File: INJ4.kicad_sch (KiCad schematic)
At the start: 8 parts, among them Q1 VND14NV04-E, Q2 VND14NV04-E, Q3 VND14NV04-E, Q4 VND14NV04-E

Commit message: Vendor DPAK/R0603 footprints for Update PCB without submodule gaps
Frame inj/LS sheets now use microcore-fp (in-repo footprints/) so KiCad
finds DPAK and R0603 even when hellen-one-common is missing from a zip
checkout. Keep hellen-one-common for Mini-B and other shared parts.
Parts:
- Q1, Q2, Q3, Q4: footprint hellen-one-common:DPAK -> microcore-fp:DPAK
- R1, R2, R3, R4: footprint hellen-one-common:R0603 -> microcore-fp:R0603
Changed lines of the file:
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@@
 			)
 		)
-		(property "Footprint" "hellen-one-common:DPAK"
+		(property "Footprint" "microcore-fp:DPAK"
 			(at 101.6 25.4 0)
 			(effects
@@
 			)
 		)
-		(property "Footprint" "hellen-one-common:R0603"
+		(property "Footprint" "microcore-fp:R0603"
 			(at 139.7 25.4 0)
 			(effects
@@
 			)
 		)
-		(property "Footprint" "hellen-one-common:DPAK"
+		(property "Footprint" "microcore-fp:DPAK"
 			(at 101.6 55.879999999999995 0)
 			(effects
@@
 			)
 		)
-		(property "Footprint" "hellen-one-common:R0603"
+		(property "Footprint" "microcore-fp:R0603"
 			(at 139.7 55.879999999999995 0)
 			(effects
@@
 			)
 		)
-		(property "Footprint" "hellen-one-common:DPAK"
+		(property "Footprint" "microcore-fp:DPAK"
 			(at 101.6 86.36 0)
 			(effects
@@
 			)
 		)
-		(property "Footprint" "hellen-one-common:R0603"
+		(property "Footprint" "microcore-fp:R0603"
 			(at 139.7 86.36 0)
 			(effects
@@
 			)
 		)
-		(property "Footprint" "hellen-one-common:DPAK"
+		(property "Footprint" "microcore-fp:DPAK"
 			(at 101.6 116.84 0)
 			(effects
@@
 			)
 		)
-		(property "Footprint" "hellen-one-common:R0603"
+		(property "Footprint" "microcore-fp:R0603"
 			(at 139.7 116.84 0)
 			(effects

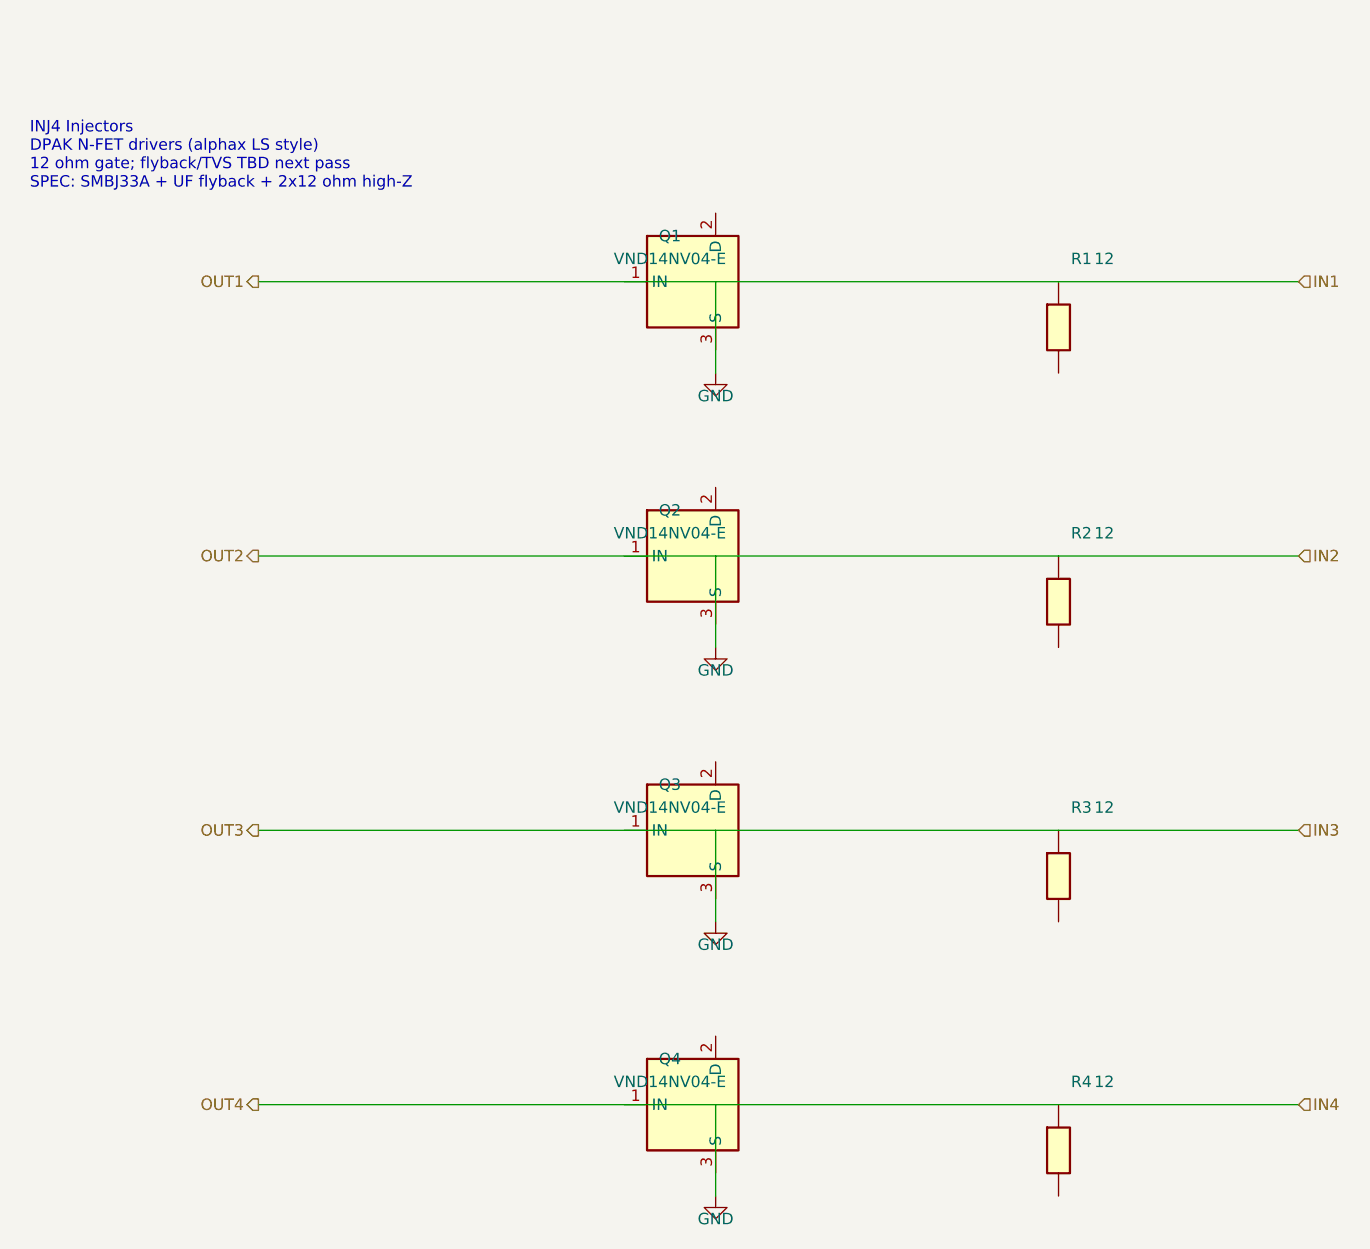
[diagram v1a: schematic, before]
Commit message: Fix top schematic wiring so labels connect to Hellen module pins
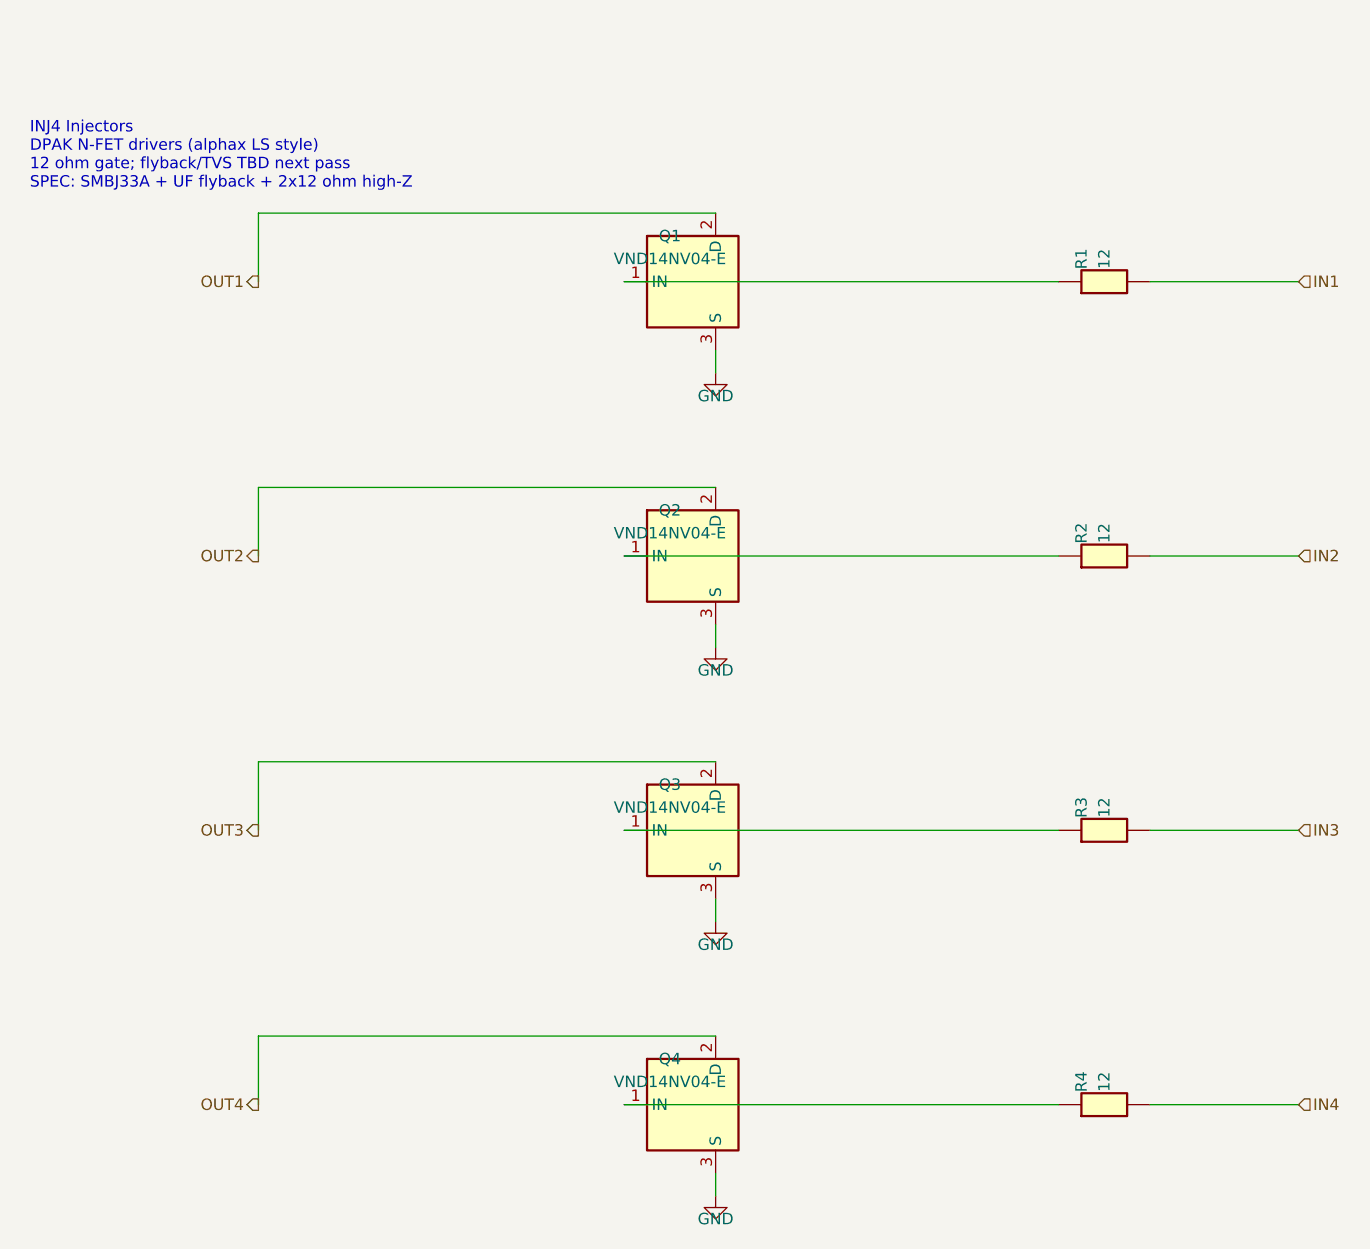
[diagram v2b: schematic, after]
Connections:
- net GND: now also Q1.3 (S), Q2.3 (S), Q3.3 (S), Q4.3 (S); no longer R1.1, R2.1, R3.1, R4.1
- net at Q4.1 (IN): now also R4.1
- net OUT4: now reaches Q4.2 (D)
- net IN1: now reaches R1.2
- net IN4: now reaches R4.2
- net IN3: now reaches R3.2
- net at Q3.1 (IN): now also R3.1
- net OUT3: now reaches Q3.2 (D)
- net at Q1.1 (IN): now also R1.1
- net OUT1: now reaches Q1.2 (D)
- net IN2: now reaches R2.2
- net at Q2.1 (IN): now also R2.1
- net OUT2: now reaches Q2.2 (D)
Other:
- moved on the sheet: R1, R2, R3, R4
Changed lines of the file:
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@@
 	(symbol
 		(lib_id "hellen-one-common:Res")
-		(at 139.7 25.4 270)
+		(at 139.7 25.4 0)
 		(unit 1)
 		(exclude_from_sim no)
@@
 	(symbol
 		(lib_id "hellen-one-common:Res")
-		(at 139.7 55.879999999999995 270)
+		(at 139.7 55.879999999999995 0)
 		(unit 1)
 		(exclude_from_sim no)
@@
 	(symbol
 		(lib_id "hellen-one-common:Res")
-		(at 139.7 86.36 270)
+		(at 139.7 86.36 0)
 		(unit 1)
 		(exclude_from_sim no)
@@
 	(symbol
 		(lib_id "hellen-one-common:Res")
-		(at 139.7 116.84 270)
+		(at 139.7 116.84 0)
 		(unit 1)
 		(exclude_from_sim no)
@@
 		)
 	)
-	(wire
-		(pts
-			(xy 50.8 25.4) (xy 101.6 25.4)
-		)
-		(stroke
-			(width 0)
-			(type default)
-		)
-	)
-	(wire
-		(pts
-			(xy 101.6 25.4) (xy 139.7 25.4)
-		)
-		(stroke
-			(width 0)
-			(type default)
-		)
-	)
-	(wire
-		(pts
-			(xy 139.7 25.4) (xy 166.37 25.4)
-		)
-		(stroke
-			(width 0)
-			(type default)
-		)
-	)
-	(wire
-		(pts
-			(xy 101.6 25.4) (xy 101.6 35.56)
-		)
-		(stroke
-			(width 0)
-			(type default)
-		)
-	)
-	(wire
-		(pts
-			(xy 50.8 55.879999999999995) (xy 101.6 55.879999999999995)
-		)
-		(stroke
-			(width 0)
-			(type default)
-		)
-	)
-	(wire
-		(pts
-			(xy 101.6 55.879999999999995) (xy 139.7 55.879999999999995)
-		)
-		(stroke
-			(width 0)
-			(type default)
-		)
-	)
-	(wire
-		(pts
-			(xy 139.7 55.879999999999995) (xy 166.37 55.879999999999995)
-		)
-		(stroke
-			(width 0)
-			(type default)
-		)
-	)
-	(wire
-		(pts
-			(xy 101.6 55.879999999999995) (xy 101.6 66.03999999999999)
-		)
-		(stroke
-			(width 0)
-			(type default)
-		)
-	)
-	(wire
-		(pts
-			(xy 50.8 86.36) (xy 101.6 86.36)
-		)
-		(stroke
-			(width 0)
-			(type default)
-		)
-	)
-	(wire
-		(pts
-			(xy 101.6 86.36) (xy 139.7 86.36)
-		)
-		(stroke
-			(width 0)
-			(type default)
-		)
-	)
-	(wire
-		(pts
-			(xy 139.7 86.36) (xy 166.37 86.36)
-		)
-		(stroke
-			(width 0)
-			(type default)
-		)
-	)
-	(wire
-		(pts
-			(xy 101.6 86.36) (xy 101.6 96.52)
-		)
-		(stroke
-			(width 0)
-			(type default)
-		)
-	)
-	(wire
-		(pts
-			(xy 50.8 116.84) (xy 101.6 116.84)
-		)
-		(stroke
-			(width 0)
-			(type default)
-		)
-	)
-	(wire
-		(pts
-			(xy 101.6 116.84) (xy 139.7 116.84)
-		)
-		(stroke
-			(width 0)
-			(type default)
-		)
-	)
-	(wire
-		(pts
-			(xy 139.7 116.84) (xy 166.37 116.84)
-		)
-		(stroke
-			(width 0)
-			(type default)
-		)
-	)
-	(wire
-		(pts
-			(xy 101.6 116.84) (xy 101.6 127.0)
-		)
-		(stroke
-			(width 0)
-			(type default)
-		)
-	)
 	(text "INJ4 Injectors\nDPAK N-FET drivers (alphax LS style)\n12 ohm gate; flyback/TVS TBD next pass\nSPEC: SMBJ33A + UF flyback + 2x12 ohm high-Z"
 		(at 25.4 15.24 0)
@@
 		)
 	)
+	(wire
+		(pts
+			(xy 50.8 25.4) (xy 50.8 17.78)
+		)
+		(stroke
+			(width 0)
+			(type default)
+		)
+	)
+	(wire
+		(pts
+			(xy 50.8 17.78) (xy 101.6 17.78)
+		)
+		(stroke
+			(width 0)
+			(type default)
+		)
+	)
+	(wire
+		(pts
+			(xy 101.6 33.02) (xy 101.6 35.56)
+		)
+		(stroke
+			(width 0)
+			(type default)
+		)
+	)
+	(wire
+		(pts
+			(xy 166.37 25.4) (xy 149.86 25.4)
+		)
+		(stroke
+			(width 0)
+			(type default)
+		)
+	)
+	(wire
+		(pts
+			(xy 139.7 25.4) (xy 91.44 25.4)
+		)
+		(stroke
+			(width 0)
+			(type default)
+		)
+	)
+	(wire
+		(pts
+			(xy 50.8 55.88) (xy 50.8 48.26)
+		)
+		(stroke
+			(width 0)
+			(type default)
+		)
+	)
+	(wire
+		(pts
+			(xy 50.8 48.26) (xy 101.6 48.26)
+		)
+		(stroke
+			(width 0)
+			(type default)
+		)
+	)
+	(wire
+		(pts
+			(xy 101.6 63.5) (xy 101.6 66.04)
+		)
+		(stroke
+			(width 0)
+			(type default)
+		)
+	)
+	(wire
+		(pts
+			(xy 166.37 55.88) (xy 149.86 55.88)
+		)
+		(stroke
+			(width 0)
+			(type default)
+		)
+	)
+	(wire
+		(pts
+			(xy 139.7 55.88) (xy 91.44 55.88)
+		)
+		(stroke
+			(width 0)
+			(type default)
+		)
+	)
+	(wire
+		(pts
+			(xy 50.8 86.36) (xy 50.8 78.74)
+		)
+		(stroke
+			(width 0)
+			(type default)
+		)
+	)
+	(wire
+		(pts
+			(xy 50.8 78.74) (xy 101.6 78.74)
+		)
+		(stroke
+			(width 0)
+			(type default)
+		)
+	)
+	(wire
+		(pts
+			(xy 101.6 93.98) (xy 101.6 96.52)
+		)
+		(stroke
+			(width 0)
+			(type default)
+		)
+	)
+	(wire
+		(pts
+			(xy 166.37 86.36) (xy 149.86 86.36)
+		)
+		(stroke
+			(width 0)
+			(type default)
+		)
+	)
+	(wire
+		(pts
+			(xy 139.7 86.36) (xy 91.44 86.36)
+		)
+		(stroke
+			(width 0)
+			(type default)
+		)
+	)
+	(wire
+		(pts
+			(xy 50.8 116.84) (xy 50.8 109.22)
+		)
+		(stroke
+			(width 0)
+			(type default)
+		)
+	)
+	(wire
+		(pts
+			(xy 50.8 109.22) (xy 101.6 109.22)
+		)
+		(stroke
+			(width 0)
+			(type default)
+		)
+	)
+	(wire
+		(pts
+			(xy 101.6 124.46) (xy 101.6 127)
+		)
+		(stroke
+			(width 0)
+			(type default)
+		)
+	)
+	(wire
+		(pts
+			(xy 166.37 116.84) (xy 149.86 116.84)
+		)
+		(stroke
+			(width 0)
+			(type default)
+		)
+	)
+	(wire
+		(pts
+			(xy 139.7 116.84) (xy 91.44 116.84)
+		)
+		(stroke
+			(width 0)
+			(type default)
+		)
+	)

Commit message: Rev j: injector SMAJ33A TVS, US1M flyback, and 2nd 12Ω per INJ channel
SPEC power-stage protection on INJ4 sch+PCB: R8–R11 ballast, D1–D4 US1M,
D5–D8 SMAJ33A (DO-214AC equivalent of SMBJ33A). FET cluster left in place;
new parts in alley + pocket C. BOARD_REVISION bumped to j. PCB remains
substantial (zones + aux origin intact).

Co-authored-by: Quintin <quintinbannink42@users.noreply.github.com>
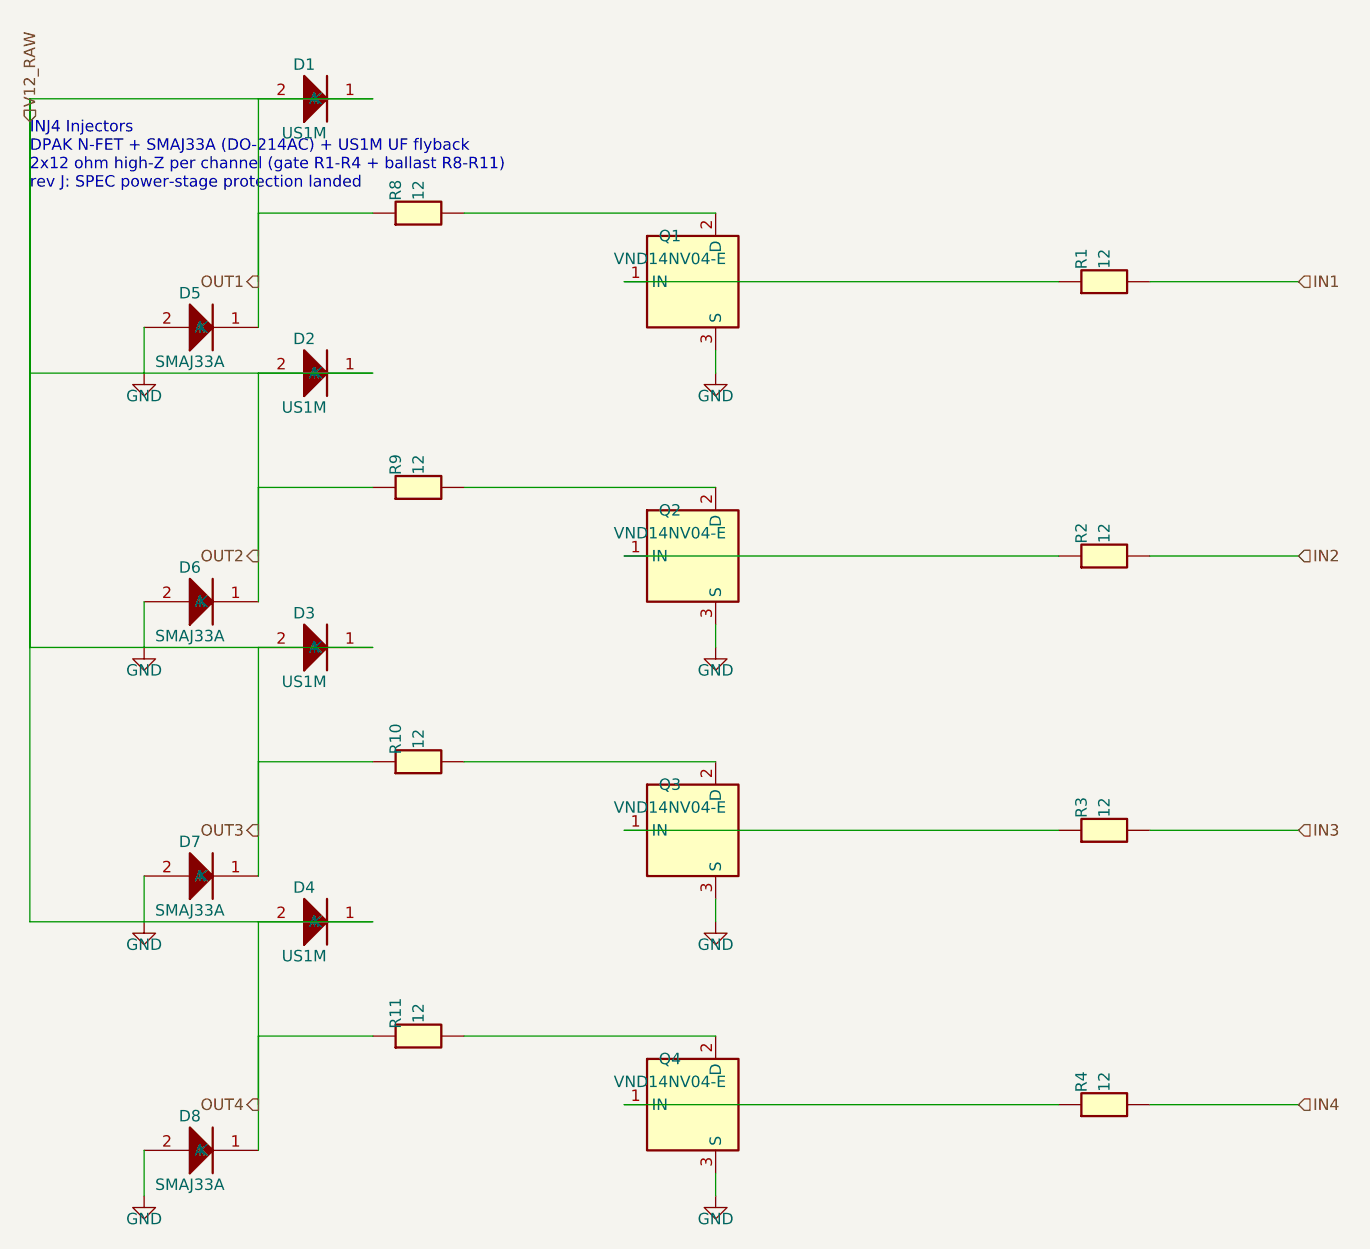
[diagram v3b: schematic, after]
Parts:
- added D1, D2, D3, D4: US1M, microcore-fp:DO214AC, symbol hellen-one-common:1N4148WS
- added D5, D6, D7, D8: SMAJ33A, microcore-fp:DO214AC, symbol hellen-one-common:1N4148WS
- added R10, R11, R8, R9: 12, microcore-fp:R0603, symbol hellen-one-common:Res
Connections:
- net GND: now also D5.2 (A), D6.2 (A), D7.2 (A), D8.2 (A)
- net OUT1: now also D1.2 (A), D5.1 (K), R8.1; no longer Q1.2 (D)
- net OUT2: now also D2.2 (A), D6.1 (K), R9.1; no longer Q2.2 (D)
- net OUT3: now also D3.2 (A), D7.1 (K), R10.1; no longer Q3.2 (D)
- net OUT4: now also D4.2 (A), D8.1 (K), R11.1; no longer Q4.2 (D)
- new net: Q4.2 (D), R11.2
- new net: Q3.2 (D), R10.2
- new net: Q2.2 (D), R9.2
- new net: Q1.2 (D), R8.2
- new net V12_RAW: D1.1 (K), D2.1 (K), D3.1 (K), D4.1 (K)
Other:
- note added: "INJ4 Injectors DPAK N-FET + SMAJ33A (DO-214AC) + US1M UF flyback 2x12 ohm high-Z per channel (gate R1-R4 + ballast R8-R11) rev J: SPEC power-stage protection landed"
- note removed: "INJ4 Injectors DPAK N-FET drivers (alphax LS style) 12 ohm gate; flyback/TVS TBD next pass SPEC: SMBJ33A + UF flyback + 2x12 ohm high-Z"

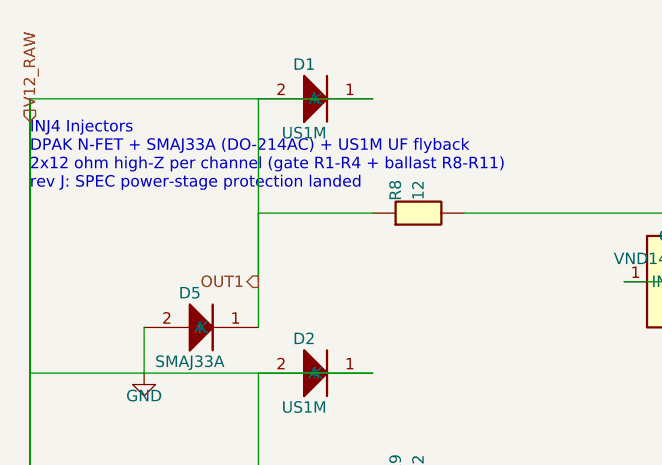
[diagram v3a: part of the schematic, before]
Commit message: Rev k: move injector diodes to B.Cu near J1; drop frame buttons
Flip D1-D4 (US1M) and D5-D8 (SMAJ33A) onto the bottom copper on the
west/east flanks of AMPSEAL J1, outside the TE_776231 silk/body keepout,
and delete the old F.Cu alley/pocket-C footprints and 0.4 mm wrap tracks.
Remove frame SW_BOOT/SW_RESET from schematic and PCB (mega-mcu100
internal buttons stay). Bump BOARD_REVISION j to k; PCB stays substantial
with Edge.Cuts drill origin unchanged.

Co-authored-by: Quintin <quintinbannink42@users.noreply.github.com>
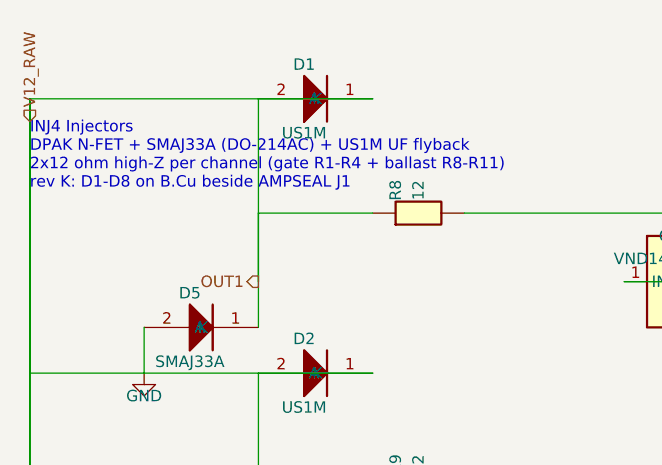
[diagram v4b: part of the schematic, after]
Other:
- note added: "INJ4 Injectors DPAK N-FET + SMAJ33A (DO-214AC) + US1M UF flyback 2x12 ohm high-Z per channel (gate R1-R4 + ballast R8-R11) rev K: D1-D8 on B.Cu beside AMPSEAL J1"
- note removed: "INJ4 Injectors DPAK N-FET + SMAJ33A (DO-214AC) + US1M UF flyback 2x12 ohm high-Z per channel (gate R1-R4 + ballast R8-R11) rev J: SPEC power-stage protection landed"
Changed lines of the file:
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@@
 		(title "INJ4 Injectors")
 		(date "2026-09-13")
-		(rev "J")
+		(rev "K")
 		(company "Core EFI")
 	)
@@
 		)
 	)
-	(text "INJ4 Injectors\nDPAK N-FET + SMAJ33A (DO-214AC) + US1M UF flyback\n2x12 ohm high-Z per channel (gate R1-R4 + ballast R8-R11)\nrev J: SPEC power-stage protection landed"
+	(text "INJ4 Injectors\nDPAK N-FET + SMAJ33A (DO-214AC) + US1M UF flyback\n2x12 ohm high-Z per channel (gate R1-R4 + ballast R8-R11)\nrev K: D1-D8 on B.Cu beside AMPSEAL J1"
 		(at 25.4 15.24 0)
 		(effects
